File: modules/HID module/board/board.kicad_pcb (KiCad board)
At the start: 2 copper layers, 40 parts, among them J1 USB_B, J2 Conn_01x06_Female, J3 Conn_02x12_Odd_Even, J4 Conn_02x12_Odd_Even, SW1 SW_Push, SW2 SW_Push, SW3 SW_Push, SW4 SW_Push, U1 AMS1117-3.3, U2 ATmega32U4-AU, U3 ESP32-WROOM-32D, Y1 16MHz

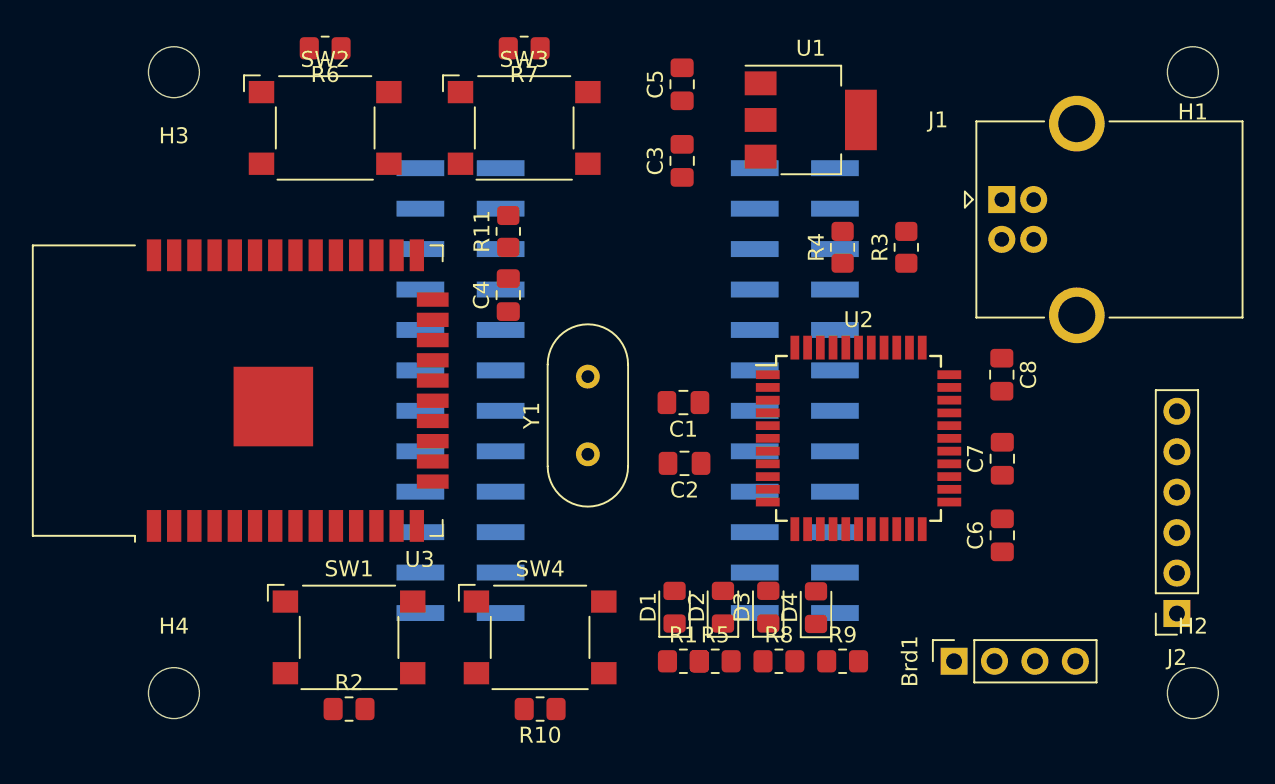
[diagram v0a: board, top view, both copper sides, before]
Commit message: HID module: Schematic and PCB layout
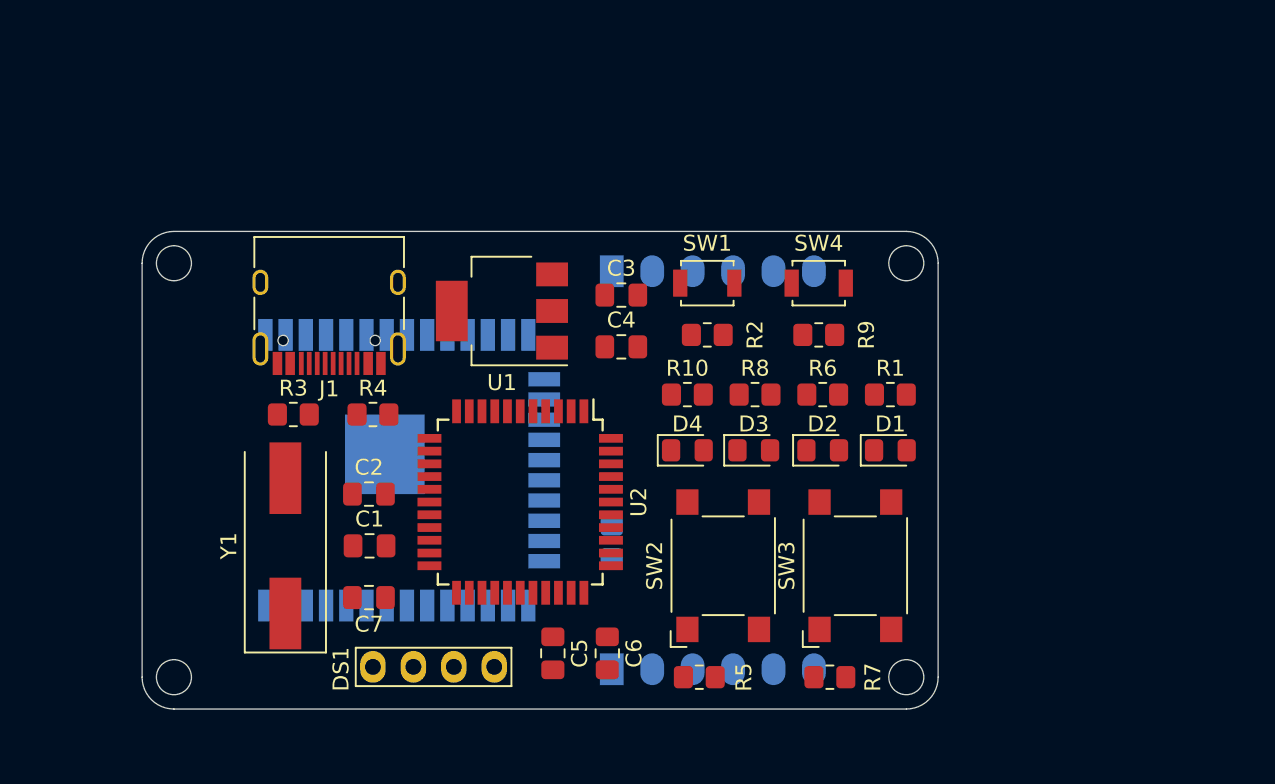
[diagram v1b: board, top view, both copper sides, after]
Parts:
- removed the C4 at (139.0, 77.0)
- removed J4: Conn_02x12_Odd_Even, Connector_PinSocket_2.54mm:PinSocket_2x12_P2.54mm_Vertical_SMD
- DS1: renamed from Brd1; footprint Connector_PinSocket_2.54mm:PinSocket_1x04_P2.54mm_Vertical -> Board:128x64OLED
- H1, H2, H3, H4: footprint MountingHole:MountingHole_3.2mm_M3 -> MountingHole:MountingHole_2.2mm_M2
- J1: value USB_B -> USB_C_Receptacle_USB2.0; footprint Connector_USB:USB_B_OST_USB-B1HSxx_Horizontal -> Connector_USB:USB_C_Receptacle_HRO_TYPE-C-31-M-12
- J2: footprint Connector_PinSocket_2.54mm:PinSocket_1x06_P2.54mm_Vertical -> Board:SolderWire_1x06_P2.54mm; moved to B.Cu
- J3: value Conn_02x12_Odd_Even -> Conn_01x06_Female; footprint Connector_PinSocket_2.54mm:PinSocket_2x12_P2.54mm_Vertical_SMD -> Board:SolderWire_1x06_P2.54mm
- R11, U3: moved to B.Cu
- SW1, SW4: footprint Button_Switch_SMD:SW_SPST_Omron_B3FS-105xP -> Button_Switch_SMD:SW_SPST_B3U-1000P
- SW2, SW3: footprint Button_Switch_SMD:SW_SPST_Omron_B3FS-105xP -> Button_Switch_SMD:SW_SPST_Omron_B3FS-100xP
- Y1: footprint Crystal:Crystal_HC49-4H_Vertical -> Crystal:Crystal_SMD_HC49-SD
- moved R5 46.0 mm to (151.0, 101.0)
- moved R7 43.9 mm to (159.2, 101.0)
- moved J1 42.7 mm to (127.8, 77.2), turned to 180 degrees
- moved C7 42.1 mm to (130.2, 96.0), turned to 180 degrees
- moved R3 39.9 mm to (125.5, 84.5), turned to 0 degrees
- moved SW2 37.2 mm to (152.5, 94.0), turned to 90 degrees
- moved J2 35.7 mm to (145.5, 100.5), turned to 270 degrees
- moved SW3 34.5 mm to (160.8, 94.0), turned to 90 degrees
- moved DS1 34.1 mm to (134.5, 89.8), turned to 180 degrees
- moved R2 32.5 mm to (151.5, 79.5), turned to 180 degrees
- moved SW1 31.6 mm to (151.5, 76.2)
- moved R4 31.3 mm to (130.5, 84.5), turned to 0 degrees
- moved R9 29.3 mm to (158.5, 79.5)
- moved C5 29.2 mm to (141.8, 99.5), turned to 270 degrees
- moved SW4 28.3 mm to (158.5, 76.2)
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- renumbered C5 to C4, C6 to C5, C7 to C6, C8 to C7, R9 to R10, R6 to R5, R5 to R6, R10 to R9
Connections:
- J3 pad 1: +5V -> (no net)
- J3 pad 2: +3V3 -> /TX
- J3 pad 3: GND -> /RX
- J3 pad 4: GND -> +3V3
- J3 pad 5: /IO21 -> (no net)
- J3 pad 6: /IO4 -> GND
- R3 pad 1: /D+ -> /D-
- R3 pad 2: Net-(J1-Pad3) -> Net-(J1-PadA7)
- R4 pad 1: /D- -> /D+
- R4 pad 2: Net-(J1-Pad2) -> Net-(J1-PadA6)
- R9 pad 2: /IO0 -> Net-(R9-Pad2)
- SW4 pad 1: /IO0 -> Net-(R9-Pad2)
- U2 pad 10: /PB2 -> (no net)
- U2 pad 11: /PB3 -> (no net)
- U2 pad 12: /PB7 -> (no net)
- U2 pad 22: /PD5 -> (no net)
- U2 pad 25: /PD4 -> (no net)
- U2 pad 26: /PD6 -> (no net)
- U2 pad 30: /PB6 -> (no net)
- U2 pad 31: /PC6 -> (no net)
- U2 pad 32: /PC7 -> (no net)
- U2 pad 36: /PF7 -> (no net)
- U2 pad 37: /PF6 -> (no net)
- U2 pad 38: /PF5 -> (no net)
- U2 pad 39: /PF4 -> (no net)
- U2 pad 40: /PF1 -> (no net)
- U2 pad 41: /PF0 -> (no net)
- U2 pad 8: /PB0 -> (no net)
- U2 pad 9: /PB1 -> (no net)
- U3 pad 10: /IO25 -> (no net)
- U3 pad 11: /IO26 -> (no net)
- U3 pad 12: /IO27 -> (no net)
- U3 pad 16: /IO13 -> (no net)
- U3 pad 23: /IO15 -> (no net)
- U3 pad 25: /IO0 -> (no net)
- U3 pad 26: /IO4 -> (no net)
- U3 pad 27: /IO16 -> (no net)
- U3 pad 28: /IO17 -> (no net)
- U3 pad 29: /IO5 -> (no net)
- U3 pad 30: /IO18 -> (no net)
- U3 pad 31: /IO19 -> (no net)
- U3 pad 33: /IO21 -> (no net)
- U3 pad 34: /PD3 -> /RX
- U3 pad 35: /PD2 -> /TX
- U3 pad 36: /IO22 -> (no net)
- U3 pad 37: /IO23 -> (no net)
- U3 pad 6: /IO34 -> (no net)
- U3 pad 7: /IO35 -> (no net)
- U3 pad 8: /IO32 -> (no net)
- U3 pad 9: /IO33 -> (no net)
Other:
- board outline added: 50 x 30 mm

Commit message: HID module: PCB complete
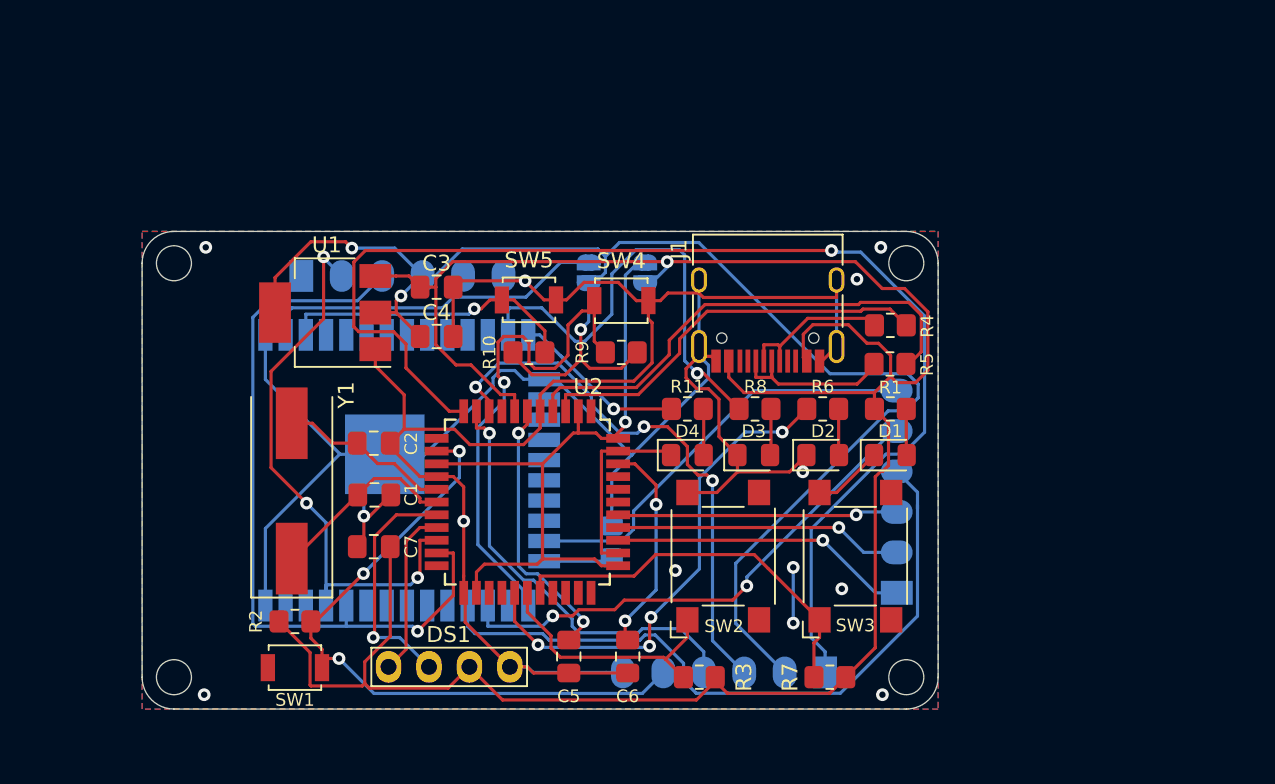
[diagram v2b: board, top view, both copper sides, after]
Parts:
- added J4: Conn_01x06_Female, Board:SolderWire_1x06_P2.54mm, B.Cu at (163.4, 95.7)
- added JP1: Jumper_NO_Small, Jumper:SolderJumper-2_P1.3mm_Open_RoundedPad1.0x1.5mm, B.Cu at (147.6, 75.6)
- added JP2: Jumper_NO_Small, Jumper:SolderJumper-2_P1.3mm_Open_RoundedPad1.0x1.5mm, B.Cu at (144.1, 75.6)
- added R10: 5k, Resistor_SMD:R_0805_2012Metric_Pad1.20x1.40mm_HandSolder, F.Cu at (140.3, 80.6)
- added SW5: SW_Push, Button_Switch_SMD:SW_SPST_B3U-1000P, F.Cu at (140.3, 77.3)
- moved R4 37.9 mm to (163.0, 78.9), turned to 180 degrees
- moved SW1 35.4 mm to (125.6, 100.4), turned to 180 degrees
- moved R5 32.6 mm to (163.0, 81.3), turned to 180 degrees
- moved R2 31.5 mm to (125.6, 97.5), turned to 0 degrees
- moved J2 31.5 mm to (126.0, 75.8)
- moved J3 28.5 mm to (158.9, 100.7), turned to 90 degrees
- moved J1 27.6 mm to (155.3, 77.1)
- moved R9 12.4 mm to (146.1, 80.6)
- moved SW4 12.4 mm to (146.1, 77.3)
- moved C4 11.6 mm to (134.5, 79.6)
- moved C3 11.6 mm to (134.5, 76.5)
- moved U1 11.1 mm to (127.5, 78.1)
- moved Y1 3.47 mm to (125.4, 89.3)
- moved C1 3.21 mm to (130.6, 89.5)
- moved C2 3.21 mm to (130.6, 86.3)
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- renumbered R10 to R11, R11 to R12, R5 to R3, R3 to R4, R4 to R5
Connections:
- net /IO12 renamed /LED-P
- net /IO14 renamed /LED-C
- net /PD0 renamed /SCL
- net /PD1 renamed /SDA
- J2 pad 2: /PD2 -> /TX
- J2 pad 3: /PD3 -> /RX
- J3 pad 1: (no net) -> /MISO
- J3 pad 2: /TX -> +3V3
- J3 pad 3: /RX -> /SCK
- J3 pad 4: +3V3 -> /MOSI
- J3 pad 5: (no net) -> /RESET
- R1 pad 1: +3V3 -> +5V
- R2 pad 1: +3V3 -> +5V
- R2 pad 2: /EN -> /RESET
- R3 pad 1: +3V3 -> +5V
- R7 pad 1: +3V3 -> +5V
- R9 pad 2: Net-(R9-Pad2) -> /IO0
- SW1 pad 1: /EN -> /RESET
- SW4 pad 1: Net-(R9-Pad2) -> /IO0
- U2 pad 10: (no net) -> /MOSI
- U2 pad 11: (no net) -> /MISO
- U2 pad 13: /EN -> /RESET
- U2 pad 14: +5V -> Net-(JP1-Pad2)
- U2 pad 2: +5V -> Net-(JP1-Pad2)
- U2 pad 20: /PD2 -> /TX
- U2 pad 21: /PD3 -> /RX
- U2 pad 24: +5V -> Net-(JP1-Pad2)
- U2 pad 34: +5V -> Net-(JP1-Pad2)
- U2 pad 36: (no net) -> /PF7
- U2 pad 37: (no net) -> /PF6
- U2 pad 38: (no net) -> /PF5
- U2 pad 44: +5V -> Net-(JP1-Pad2)
- U2 pad 9: (no net) -> /SCK
- U3 pad 2: +3V3 -> Net-(JP2-Pad2)
- U3 pad 23: (no net) -> /IO15
- U3 pad 25: (no net) -> /IO0
- U3 pad 27: (no net) -> /IO16
- U3 pad 28: (no net) -> /IO17
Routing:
- net GND: track 0.00 -> 213.3 mm, vias 0 -> 13
- net +5V: track 0.00 -> 148.8 mm, vias 0 -> 1
- net +3V3: track 0.00 -> 97.5 mm, vias 0 -> 3
- net /MISO: track 0.00 -> 78.3 mm, vias 0 -> 1
- net /RX: track 0.00 -> 47.2 mm, vias 0 -> 1
- net /IO17: track 0.00 -> 44.1 mm
- net Net-(JP1-Pad2): track 0.00 -> 42.6 mm, vias 0 -> 1
- net /RESET: track 0.00 -> 42.4 mm, vias 0 -> 3
- net /TX: track 0.00 -> 37.2 mm, vias 0 -> 3
- net /SCK: track 0.00 -> 34.6 mm, vias 0 -> 3
- net /IO0: track 0.00 -> 33.2 mm, vias 0 -> 1
- net /IO16: track 0.00 -> 32.6 mm, vias 0 -> 2
- net /LED-K: track 0.00 -> 31.4 mm, vias 0 -> 4
- net /D+: track 0.00 -> 31.1 mm
- net /LED-C: track 0.00 -> 28.9 mm, vias 0 -> 1
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- added copper zone on B.Cu, net GND
- added copper zone on F.Cu, net GND
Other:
- net class Default: trace_width 0.25 -> 0.2

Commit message: HID module: PCB modular
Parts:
- R4, R5: footprint Resistor_SMD:R_0805_2012Metric_Pad1.20x1.40mm_HandSolder -> Resistor_SMD:R_0603_1608Metric
- moved R4 1.77 mm to (164.3, 80.1), turned to 90 degrees
- moved R5 1.51 mm to (162.1, 80.1), turned to 90 degrees
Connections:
- net Net-(J1-PadA6) renamed /_D+
- net Net-(J1-PadA7) renamed /_D-
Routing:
- net /MISO: track 78.3 -> 37.7 mm, vias 1 -> 3
- net Net-(C6-Pad1): track 13.5 -> 47.1 mm, vias 2 -> 0
- net Net-(C5-Pad1): track 17.1 -> 31.3 mm, vias 2 -> 4
- net /IO17: track 44.1 -> 58.1 mm
- net GND: track 213.3 -> 224.1 mm, vias 13 -> 5
- net +5V: track 148.8 -> 158.9 mm, vias 1 -> 4
- net /IO16: track 32.6 -> 42.2 mm, vias 2 -> 0
- net /LED-K: track 31.4 -> 24.4 mm, vias 4 -> 2
- net /D+: track 31.1 -> 25.1 mm
- net /_D-: track 9.85 -> 13.8 mm
- net /SCL: track 15.1 -> 11.9 mm, vias 1 -> 0
- net /MOSI: track 27.1 -> 30.1 mm, vias 1 -> 3
- net /XTAL2: track 10.8 -> 13.7 mm
- net /SDA: track 10.6 -> 12.9 mm
- net /RX: track 47.2 -> 45.0 mm
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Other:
- board text added: "InputBlackBoxOutput"

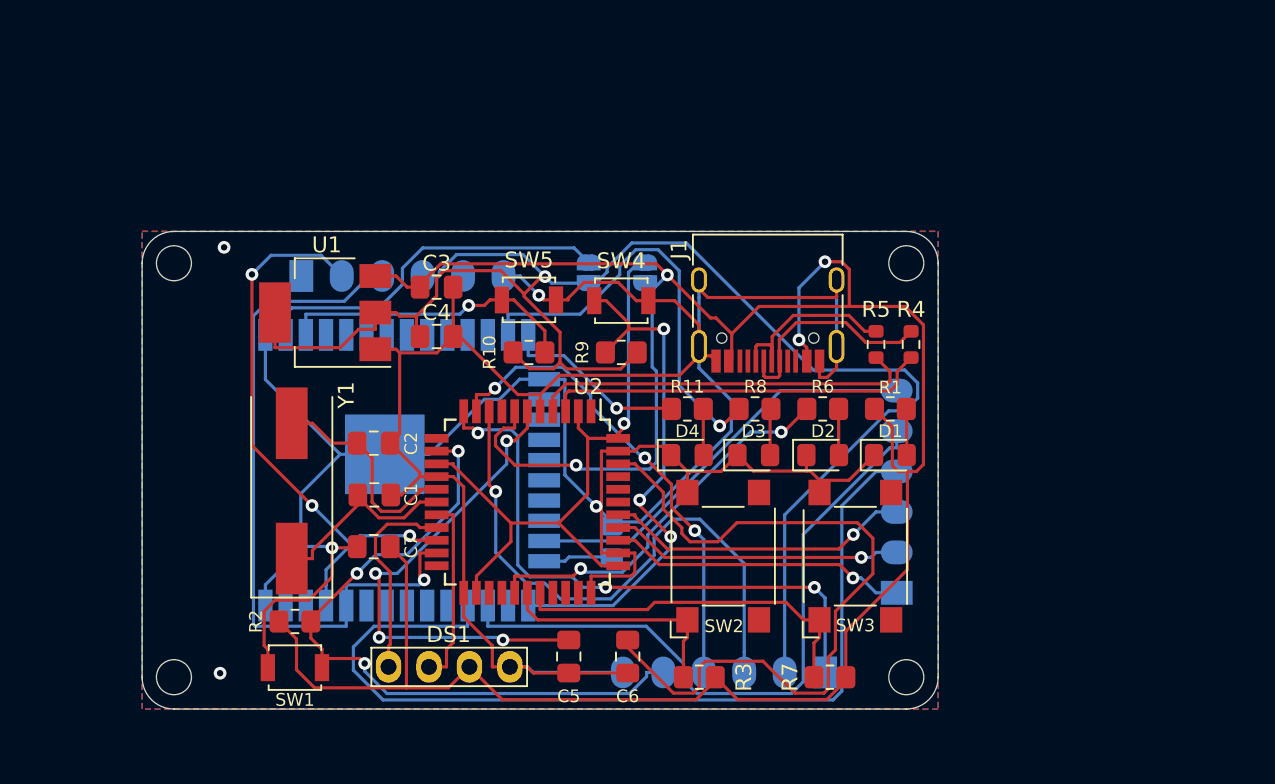
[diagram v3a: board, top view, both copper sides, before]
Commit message: PCB: USB receptacle moved closer to PCB edge
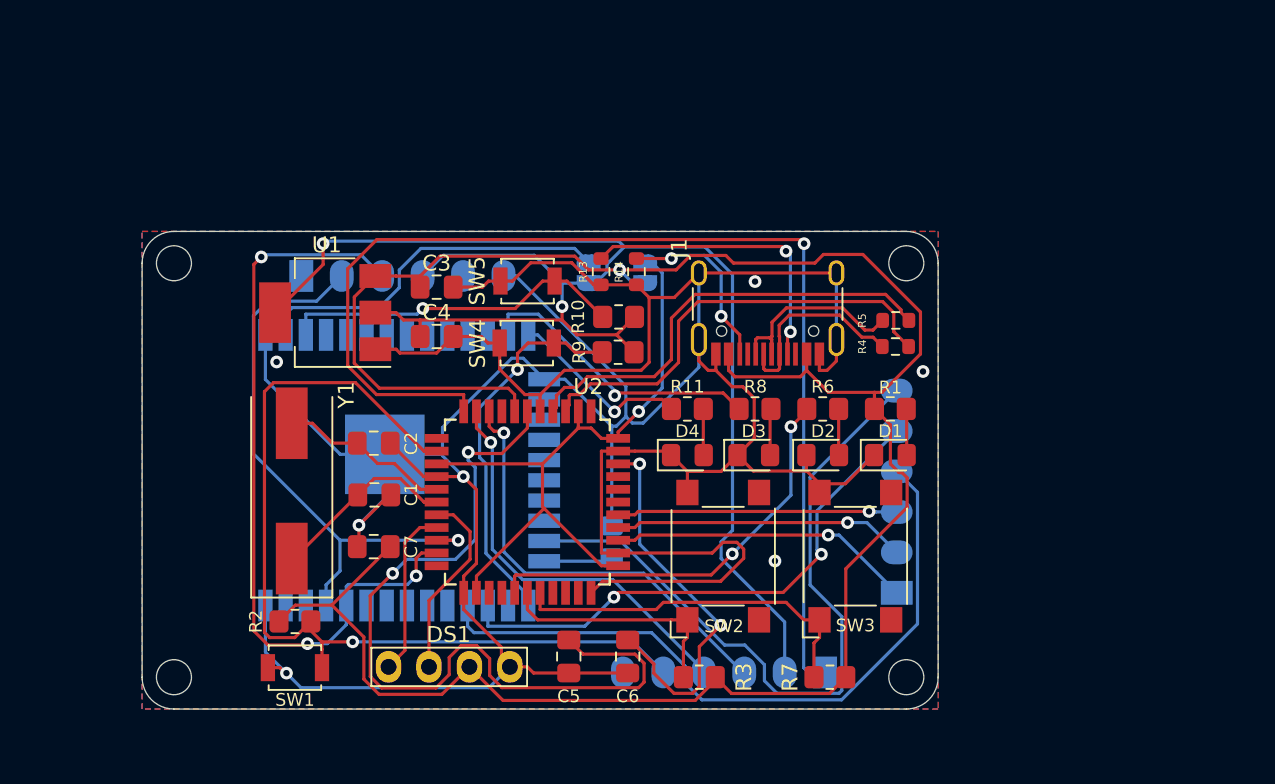
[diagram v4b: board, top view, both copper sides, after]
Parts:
- added R13: 5k1, Resistor_SMD:R_0603_1608Metric, F.Cu at (144.8, 75.5)
- added R14: 5k1, Resistor_SMD:R_0603_1608Metric, F.Cu at (147.1, 75.5)
- J1: footprint Connector_USB:USB_C_Receptacle_HRO_TYPE-C-31-M-12 -> Board:USB_C_Receptacle_HRO_TYPE-C-31-M-12
- moved SW4 6.51 mm to (140.2, 80.0), turned to 180 degrees
- moved R10 6.06 mm to (145.9, 78.4), turned to 180 degrees
- moved R5 1.95 mm to (163.3, 78.6), turned to 180 degrees
- moved SW5 1.18 mm to (140.2, 76.1), turned to 180 degrees
- moved R4 0.99 mm to (163.3, 80.2), turned to 180 degrees
- moved J1 0.44 mm to (155.3, 76.7)
- moved R9 0.20 mm to (145.9, 80.6)
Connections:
- J1 pad A5: (no net) -> Net-(J1-PadA5)
- J1 pad B5: (no net) -> Net-(J1-PadB5)
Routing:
- net /MISO: track 37.7 -> 72.5 mm, vias 3 -> 1
- net Net-(C6-Pad1): track 47.1 -> 24.4 mm, vias 0 -> 2
- net Net-(C5-Pad1): track 31.3 -> 51.9 mm, vias 4 -> 2
- net GND: track 224.1 -> 243.6 mm, vias 5 -> 7
- net /IO15: track 26.1 -> 45.2 mm
- net Net-(J1-PadA5): track 0.00 -> 18.7 mm, vias 0 -> 2
- net /IO17: track 58.1 -> 44.2 mm
- net +5V: track 158.9 -> 145.3 mm, vias 4 -> 1
- net /RESET: track 43.6 -> 56.7 mm, vias 3 -> 1
- net Net-(J1-PadB5): track 0.00 -> 11.5 mm, vias 0 -> 2
- net /IO0: track 33.0 -> 23.9 mm, vias 3 -> 1
- net /SCK: track 36.6 -> 27.7 mm
- net /LED-C: track 27.1 -> 18.6 mm
- net /IO16: track 42.2 -> 34.0 mm, vias 0 -> 2
- net /MOSI: track 30.1 -> 25.6 mm, vias 3 -> 1
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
